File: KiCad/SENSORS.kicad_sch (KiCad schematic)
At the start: 9 parts, among them J25 Screw_Terminal_01x02, U1 TMP102xxDRL, U2 A1104xLH

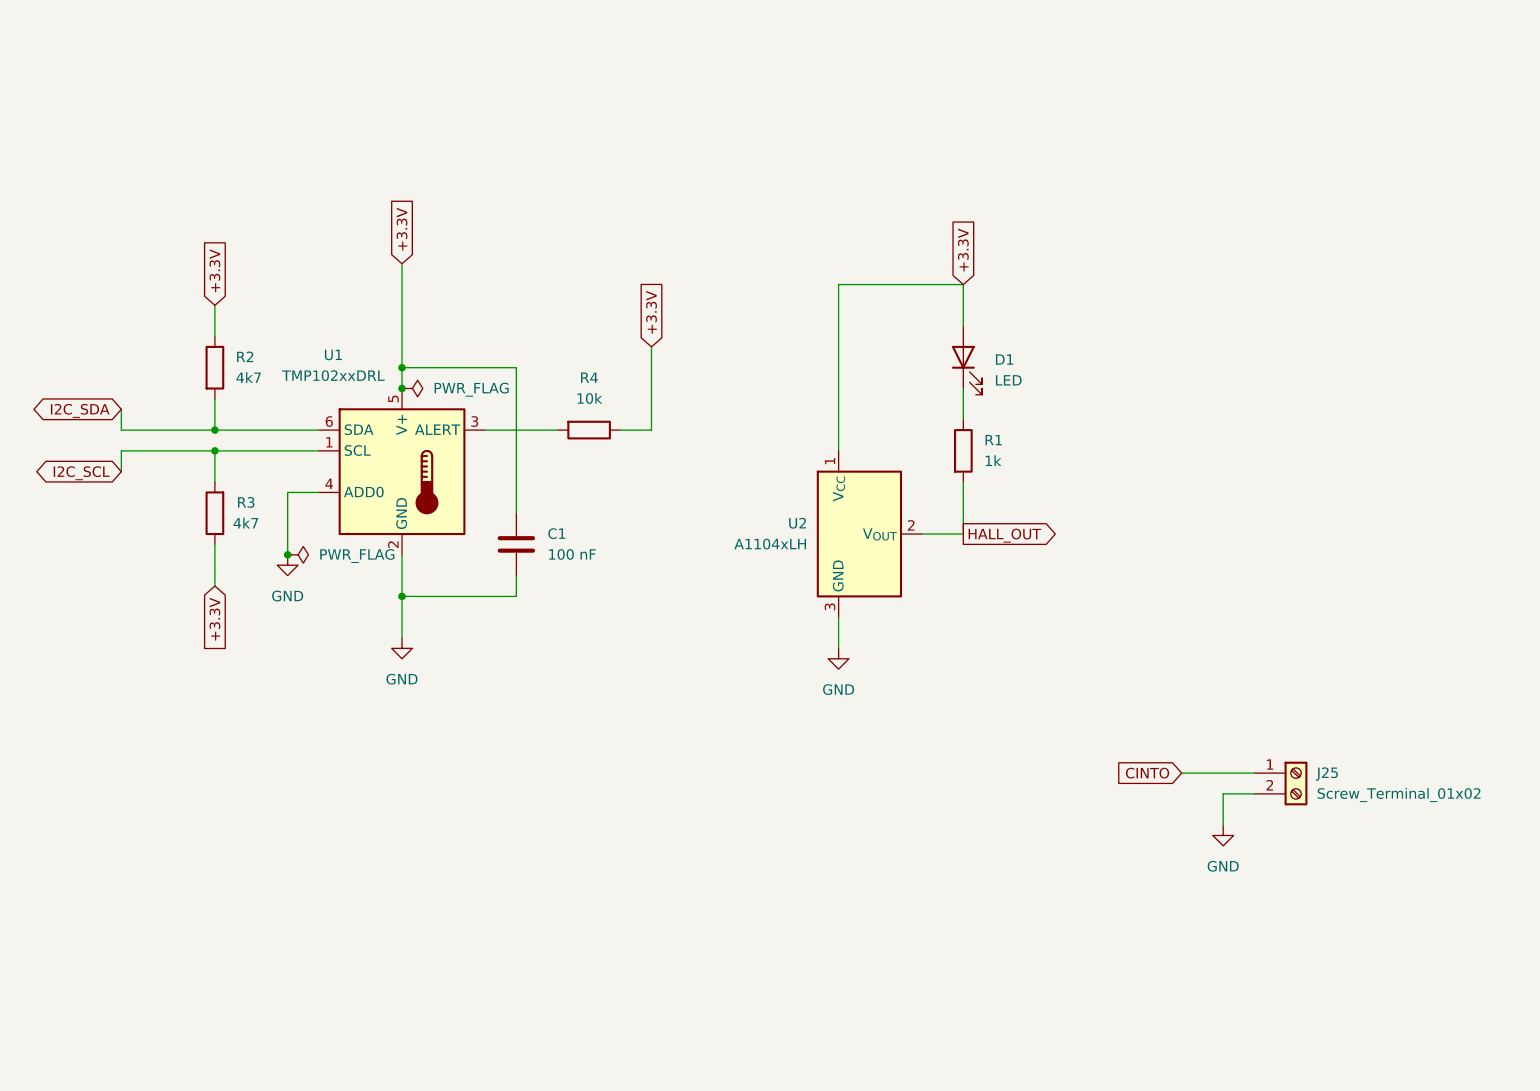
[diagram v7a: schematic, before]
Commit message: canvia al microcontrolador
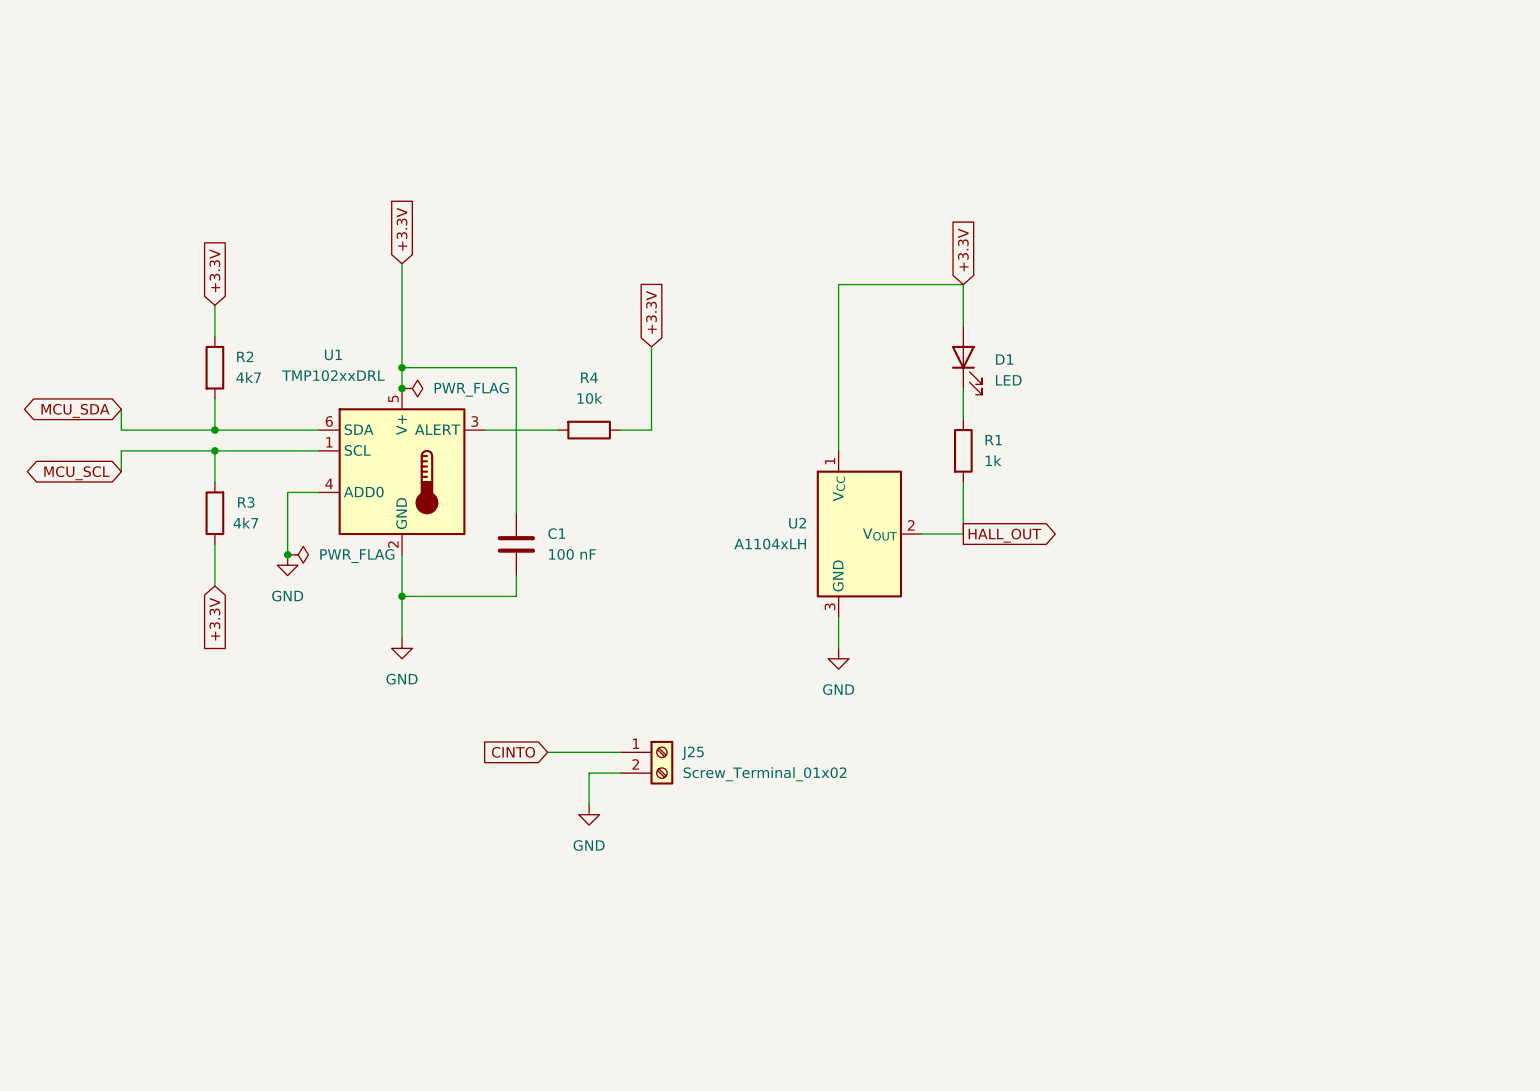
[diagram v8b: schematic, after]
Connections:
- net I2C_SCL renamed MCU_SCL
- net I2C_SDA renamed MCU_SDA
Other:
- moved on the sheet: J25
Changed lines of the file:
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@@
 	(wire
 		(pts
-			(xy 200.66 125.73) (xy 200.66 129.54)
+			(xy 123.19 123.19) (xy 123.19 127)
 		)
 		(stroke
@@
 	(wire
 		(pts
-			(xy 195.58 123.19) (xy 204.47 123.19)
+			(xy 118.11 120.65) (xy 127 120.65)
 		)
 		(stroke
@@
 	(wire
 		(pts
-			(xy 204.47 125.73) (xy 200.66 125.73)
+			(xy 127 123.19) (xy 123.19 123.19)
 		)
 		(stroke
@@
 		)
 	)
-	(global_label "I2C_SDA"
+	(global_label "MCU_SDA"
 		(shape bidirectional)
 		(at 66.04 78.74 180)
@@
 		)
 		(property "Intersheetrefs" "${INTERSHEET_REFS}"
-			(at 54.3235 78.74 0)
+			(at 53.3559 78.74 0)
 			(effects
 				(font
@@
 		)
 	)
-	(global_label "I2C_SCL"
+	(global_label "MCU_SCL"
 		(shape bidirectional)
 		(at 66.04 86.36 180)
@@
 		)
 		(property "Intersheetrefs" "${INTERSHEET_REFS}"
-			(at 54.384 86.36 0)
+			(at 53.4164 86.36 0)
 			(effects
 				(font
@@
 	(global_label "CINTO"
 		(shape input)
-		(at 195.58 123.19 180)
+		(at 118.11 120.65 180)
 		(fields_autoplaced yes)
 		(effects
@@
 		)
 		(property "Intersheetrefs" "${INTERSHEET_REFS}"
-			(at 187.0914 123.19 0)
+			(at 109.6214 120.65 0)
 			(effects
 				(font
@@
 	(symbol
 		(lib_id "Connector:Screw_Terminal_01x02")
-		(at 209.55 123.19 0)
+		(at 132.08 120.65 0)
 		(unit 1)
 		(exclude_from_sim no)
@@
 		(fields_autoplaced yes)
 		(property "Reference" "J25"
-			(at 212.09 123.1899 0)
+			(at 134.62 120.6499 0)
 			(effects
 				(font
@@
 		)
 		(property "Value" "Screw_Terminal_01x02"
-			(at 212.09 125.7299 0)
+			(at 134.62 123.1899 0)
 			(effects
 				(font
@@
 		)
 		(property "Footprint" ""
-			(at 209.55 123.19 0)
+			(at 132.08 120.65 0)
 			(effects
 				(font
@@
 		)
 		(property "Datasheet" "~"
-			(at 209.55 123.19 0)
+			(at 132.08 120.65 0)
 			(effects
 				(font
@@
 		)
 		(property "Description" "Generic screw terminal, single row, 01x02, script generated (kicad-library-utils/schlib/autogen/connector/)"
-			(at 209.55 123.19 0)
+			(at 132.08 120.65 0)
 			(effects
 				(font
@@
 	(symbol
 		(lib_id "power:GND")
-		(at 200.66 129.54 0)
+		(at 123.19 127 0)
 		(unit 1)
 		(exclude_from_sim no)
@@
 		(fields_autoplaced yes)
 		(property "Reference" "#PWR04"
-			(at 200.66 135.89 0)
+			(at 123.19 133.35 0)
 			(effects
 				(font
@@
 		)
 		(property "Value" "GND"
-			(at 200.66 134.62 0)
+			(at 123.19 132.08 0)
 			(effects
 				(font
@@
 		)
 		(property "Footprint" ""
-			(at 200.66 129.54 0)
+			(at 123.19 127 0)
 			(effects
 				(font
@@
 		)
 		(property "Datasheet" ""
-			(at 200.66 129.54 0)
+			(at 123.19 127 0)
 			(effects
 				(font
@@
 		)
 		(property "Description" "Power symbol creates a global label with name \"GND\" , ground"
-			(at 200.66 129.54 0)
-			(effects
-				(font
+			(at 123.19 127 0)
+			(effects
+				(font
